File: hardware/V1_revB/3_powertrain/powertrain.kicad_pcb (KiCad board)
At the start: 2 copper layers, 39.1 x 44.7 mm, 25 parts, among them J6 , SW1 SKRHADE010

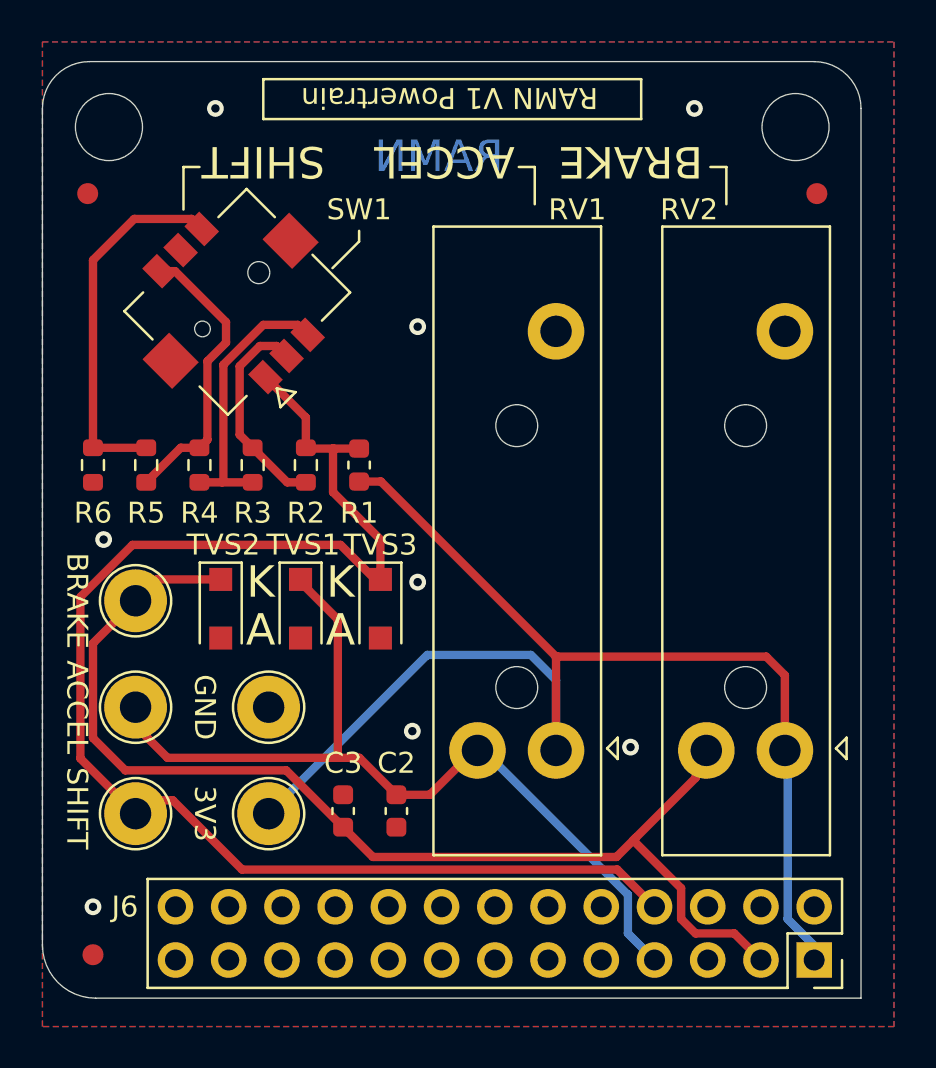
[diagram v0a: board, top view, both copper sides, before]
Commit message: 3_powertrain: import changes for the pot sliders available from PCBway
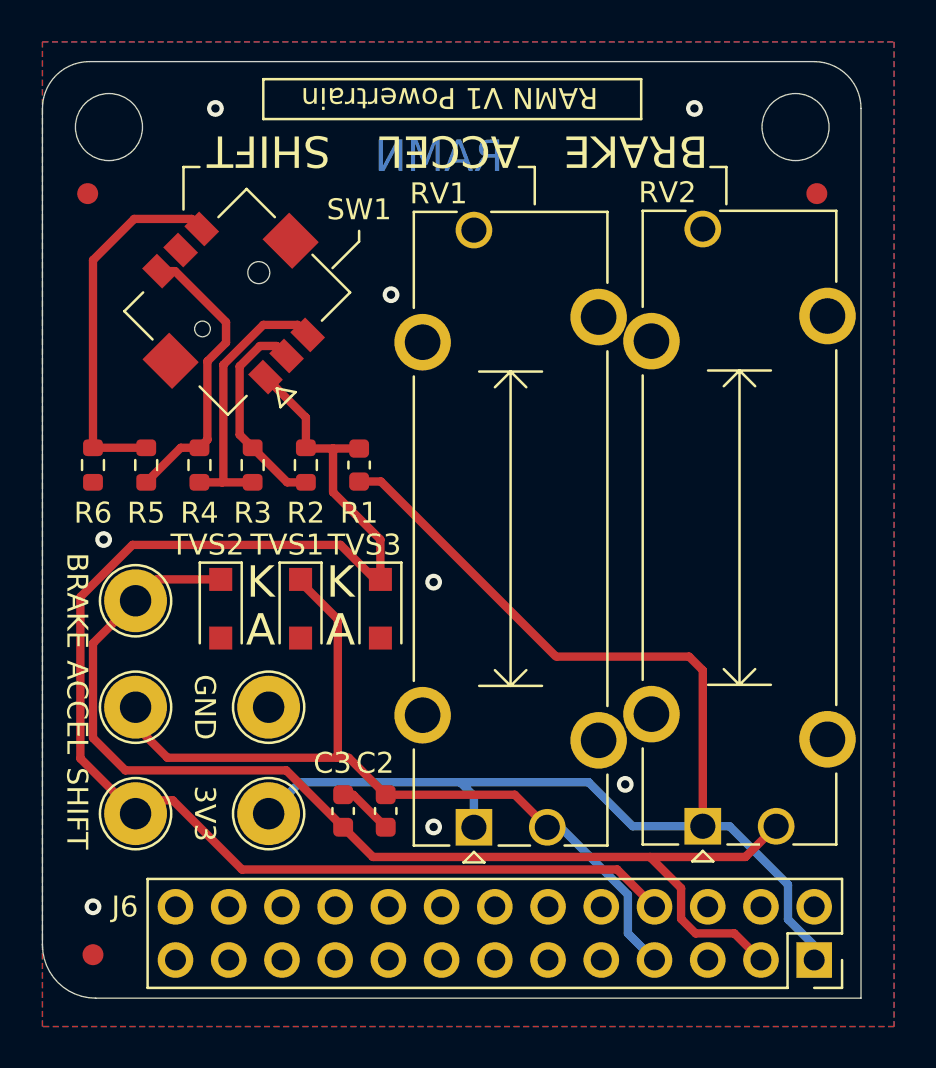
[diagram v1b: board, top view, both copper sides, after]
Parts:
- RV1, RV2: footprint custom:RS15111A900B -> Potentiometer_THT:Potentiometer_Bourns_PTA1543_Single_Slide
- moved RV1 10.4 mm to (53.0, 57.2)
- moved RV2 10.4 mm to (63.9, 57.1)
- moved C2 0.51 mm to (48.8, 56.4)
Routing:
- net GND: track 0.00 -> 2.67 mm
- net Accel: track 42.5 -> 40.1 mm
- net /3V3_ECU: track 63.7 -> 61.5 mm
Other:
- net class Default removed
